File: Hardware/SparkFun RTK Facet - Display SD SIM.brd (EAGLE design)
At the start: 50 x 22 mm, 43 parts, among them J1 FPC_12_0.5MM_BACKFLIP, J16 microSD, J17 NANO_SIM, J2 FPC_12_0.5MM_BACKFLIP, U13 LIS2DH12

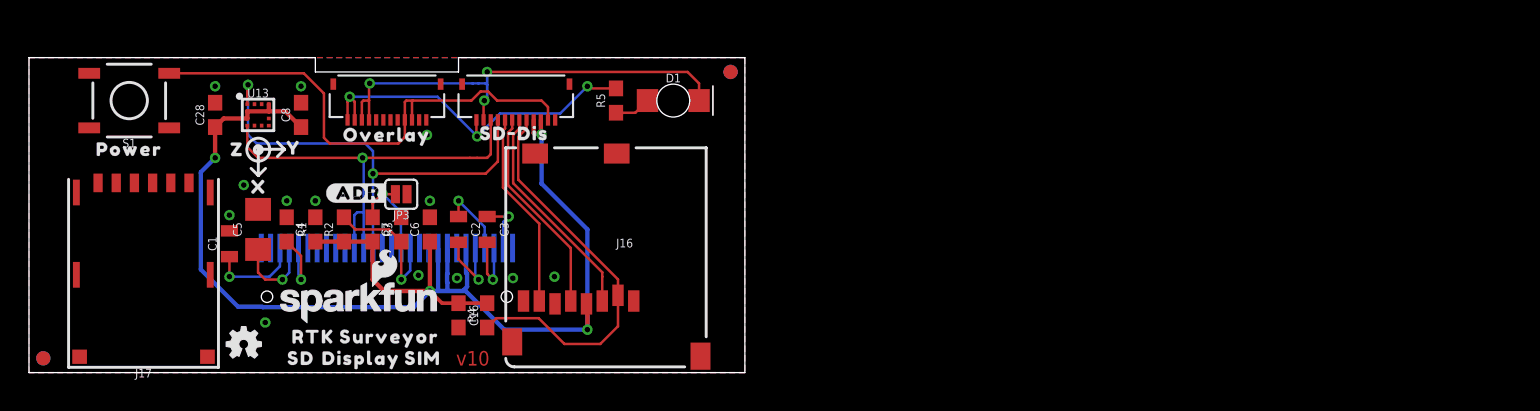
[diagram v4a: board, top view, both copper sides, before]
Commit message: Move overlay connector further down. Invert overlay connector pins.
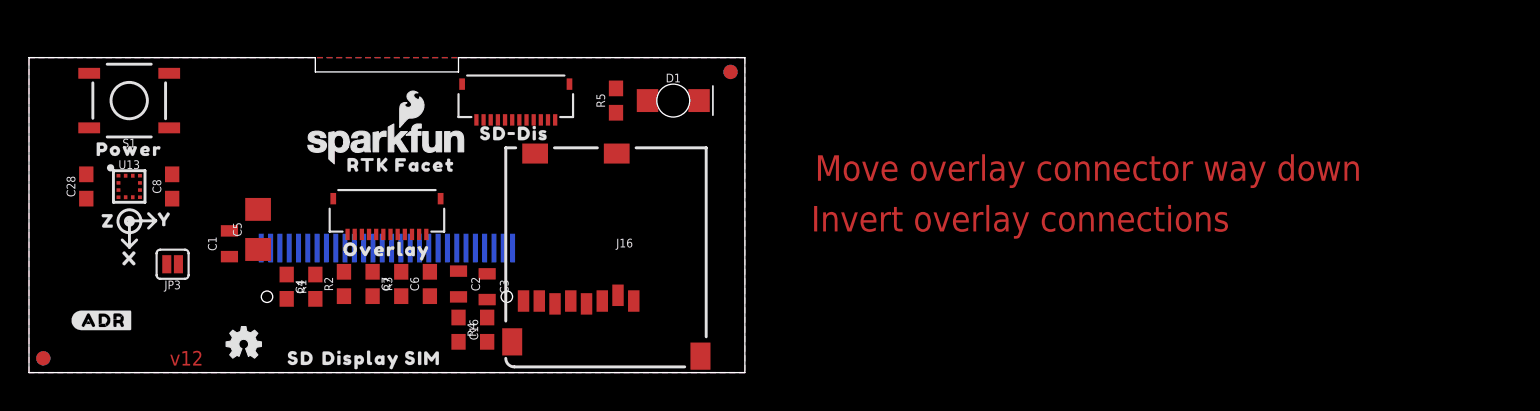
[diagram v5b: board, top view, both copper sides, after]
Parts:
- removed J17: NANO_SIM, ublox:NANO_SIM_WURTH_693043020611
- removed J2: FPC_12_0.5MM_BACKFLIP, RTK Facet:FPC_12_DOUBLESIDED_BACKFLIP
- removed U$6: (no value), output:RTK_SURVEYOR0
- added J3: FPC_12_0.5MM_BACKFLIP, RTK Facet:FPC_12_DOUBLESIDED_BACKFLIP
- added U$13: (no value), output:RTK_FACET0
- moved U$7 19.9 mm to (5.22, 3.65)
- moved JP3 16.7 mm to (10.0, 7.57)
- moved LOGO5 11.3 mm to (25.0, 16.0)
- moved C28 10.3 mm to (4.00, 13.0)
- moved C8 10.3 mm to (10.0, 13.0)
- moved U$10 10.3 mm to (6.90, 8.00)
- moved U$11 10.3 mm to (9.50, 10.7)
- moved U$12 10.3 mm to (5.40, 10.6)
- moved U13 10.3 mm to (7.00, 13.0)
- moved U$2 8.00 mm to (25.0, 8.60)
- moved C3 4.00 mm to (32.0, 6.00)
- moved C4 4.00 mm to (20.0, 6.00)
- moved R1 4.00 mm to (18.0, 6.00)
- moved C2 3.81 mm to (30.0, 6.19)
- moved C6 3.81 mm to (28.0, 6.19)
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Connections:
- net CHARGE_LED: now also J3.3, J3.4; no longer J2.10, J2.9
- net GND: now also J3.11, J3.12; no longer J2.1, J2.2
- net POWER_BTN: now also J3.10, J3.9; no longer J2.3, J2.4
- net V_USB: now also J3.1, J3.2; no longer J2.11, J2.12
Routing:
- net 3.3V: track 95.0 -> 0.00 mm, vias 4 -> 0
- net POWER_BTN: track 36.0 -> 0.00 mm
- net ESP_22/SCL: track 32.8 -> 0.00 mm, vias 2 -> 0
- net CHARGE_LED: track 32.4 -> 0.00 mm, vias 3 -> 0
- net ESP_21/SDA: track 30.7 -> 0.00 mm, vias 1 -> 0
- net SD_!CS!: track 28.2 -> 0.00 mm
- net V_USB: track 25.9 -> 0.00 mm, vias 3 -> 0
- net SD_COPI: track 15.4 -> 0.00 mm
- net SD_SCK: track 14.6 -> 0.00 mm
- net SD_CIPO: track 13.8 -> 0.00 mm
- net RESET: track 9.84 -> 0.00 mm, vias 1 -> 0
- net D/C: track 7.19 -> 0.00 mm, vias 1 -> 0
- net VCC: track 6.50 -> 0.00 mm, vias 1 -> 0
- net VCOMH: track 5.90 -> 0.00 mm, vias 1 -> 0
- net N$2: track 5.47 -> 0.00 mm, vias 1 -> 0
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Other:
- board text added: "Invert overlay connections"
- board text added: "Move overlay connector way down"
- board text added: "v12"
- board text removed: "v10"
